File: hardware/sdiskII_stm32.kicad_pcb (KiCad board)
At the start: 2 copper layers, 76 x 56.3 mm, 23 parts, among them J1 PWR, J2 APPLE_SDISKII, J3 Conn_01x06, J4 UART, J5 Conn_01x04, J6 STLINK, U2 MicroSD_SDIO, U8 DM-OLED096-636

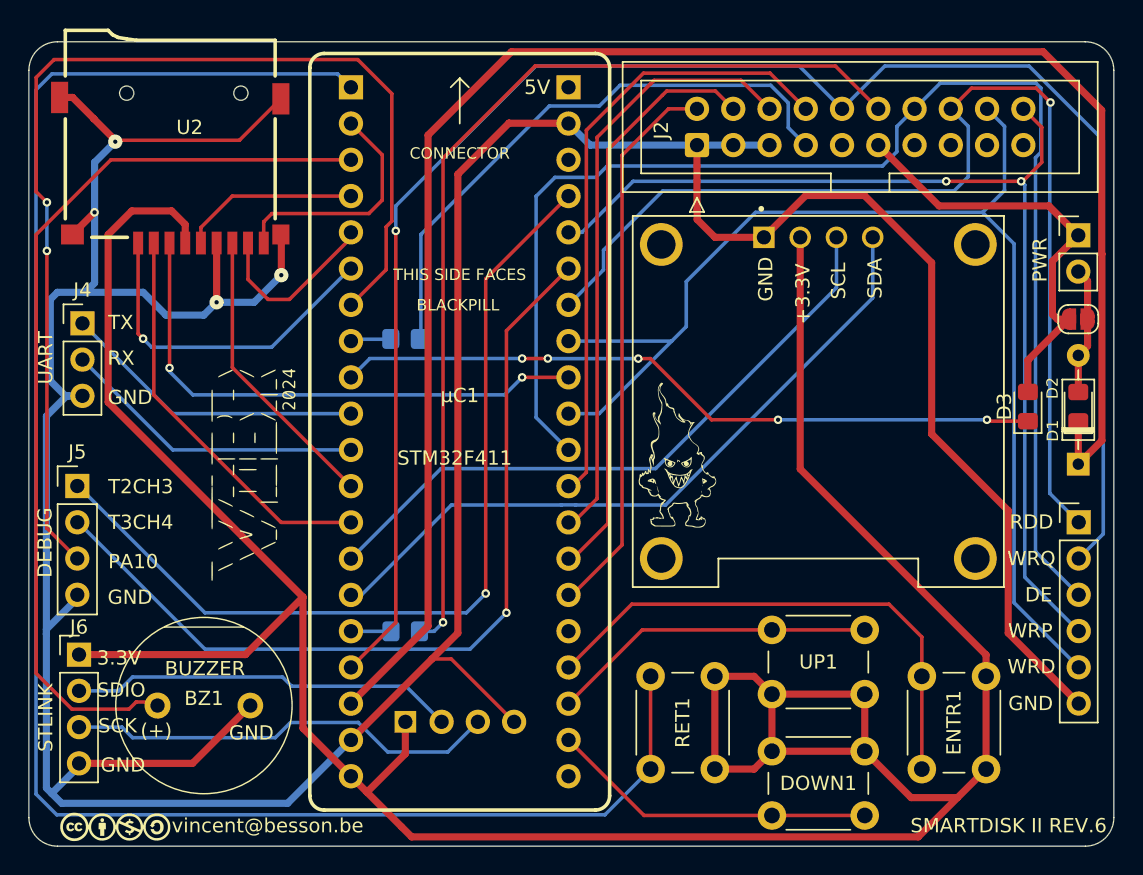
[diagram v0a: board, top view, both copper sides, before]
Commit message: fixing Smartport on IIe II+ Rev6 Hardware
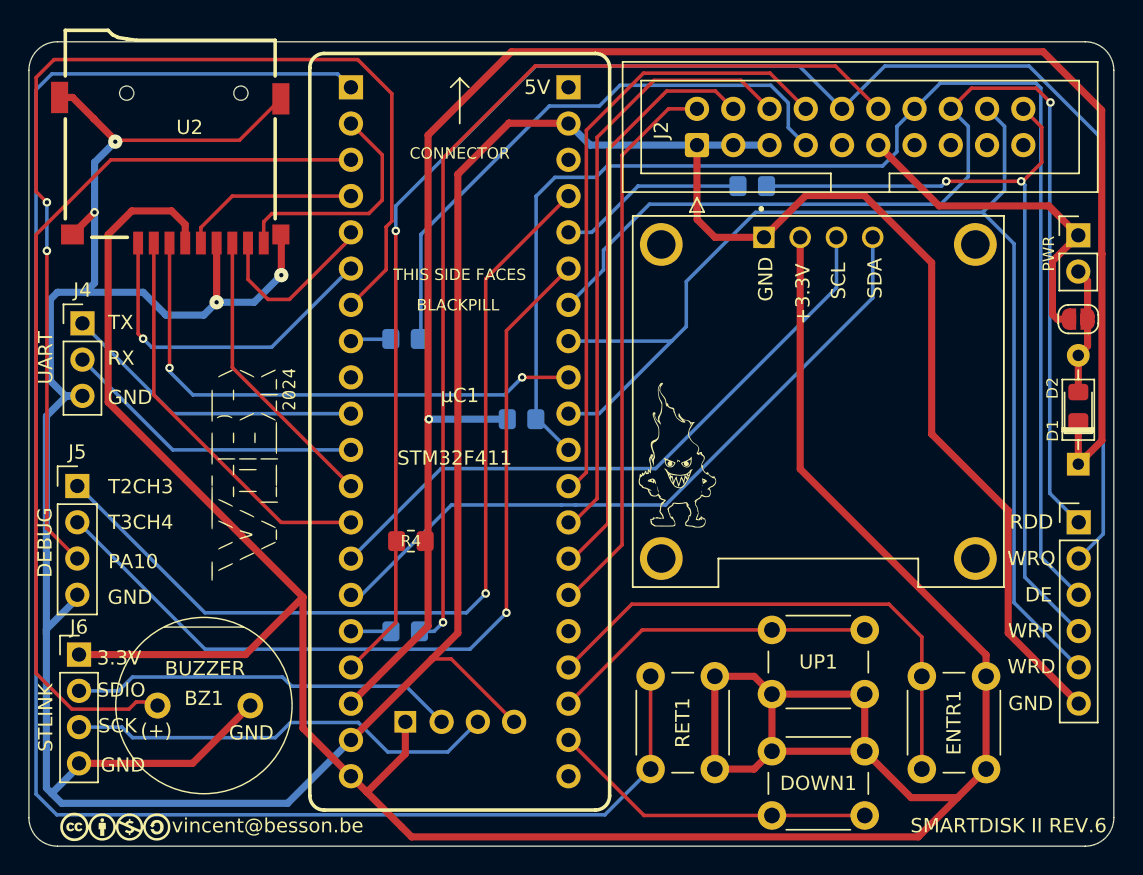
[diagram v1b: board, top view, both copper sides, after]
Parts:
- removed D3: 1N4148WT, Diode_SMD:D_0805_2012Metric_Pad1.15x1.40mm_HandSolder
- added R1: 330, Resistor_SMD:R_0805_2012Metric_Pad1.20x1.40mm_HandSolder, B.Cu at (182.2, 95.4)
- added R4: 1K5, Resistor_SMD:R_0805_2012Metric_Pad1.20x1.40mm_HandSolder, F.Cu at (158.2, 120.2)
- added R5: 1K5, Resistor_SMD:R_0805_2012Metric_Pad1.20x1.40mm_HandSolder, B.Cu at (166.0, 111.7)
- renumbered R5 to R2, R4 to R3
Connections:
- J2 pad 20: WR_PROTECT -> WR_PROTECT_D
- J3 pad 4: WR_PROTECT -> WR_PROTECT_D
- μC1 pad 9: A2PWR -> unconnected-(μC1-A12-Pad9)
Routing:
- net WR_PROTECT: track 72.6 -> 13.2 mm, vias 2 -> 0
- net WR_PROTECT_D: track 0.00 -> 57.4 mm, vias 0 -> 2
- net A2PWR: track 49.8 -> 0.00 mm, vias 5 -> 0
- net VCC: track 30.7 -> 24.4 mm
- net PWR_IN: track 121.9 -> 127.4 mm, vias 0 -> 1
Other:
- board text added: "REV6: (beta) #2 - Adding R6 on WR_PROTECT for future use - Adding PUP On DEVICE_ENABLE, WR_REQ - Adding D3, to avoid PA12 -> Apple PWR supply REV5: (beta) - Adding D1 & D2 protection (only one is needed), - Adding more GND to SDCARD - Adding R4 PIN SELECT for protection on DISK3.5 use - Adding R5 PIN SELECT for protection on DISK3.5 use REV4: (Last production & tested version) - Adding PWR pads -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"
- board text removed: "REV6: (beta) - Adding A2PWR PA12, Apple II PWR check on external PWR supply - Adding D3, to avoid PA12 -> Apple PWR supply REV5: (beta) - Adding D1 & D2 protection (only one is needed), - Adding more GND to SDCARD - Adding R4 PIN SELECT for protection on DISK3.5 use - Adding R5 PIN SELECT for protection on DISK3.5 use REV4: (Last production & tested version) - Adding PWR pads - Moving SDCard"

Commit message: Board rev7 beta
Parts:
- removed the   at (147.0, 115.5)
- added 3V: SPST, Jumper:SolderJumper-2_P1.3mm_Open_RoundedPad1.0x1.5mm, F.Cu at (142.1, 121.2)
- added 3V: PWR, Connector_PinHeader_2.54mm:PinHeader_1x02_P2.54mm_Vertical, F.Cu at (138.7, 122.7)
- added C1: 10uF, Capacitor_SMD:C_0805_2012Metric_Pad1.18x1.45mm_HandSolder, F.Cu at (138.4, 116.0)
- added C2: 10uF, Capacitor_SMD:C_0805_2012Metric_Pad1.18x1.45mm_HandSolder, F.Cu at (149.4, 106.7)
- added Fu2: Polyfuse 500mA, Fuse:Fuse_0805_2012Metric_Pad1.15x1.40mm_HandSolder, F.Cu at (204.7, 109.4)
- added G***: LOGO, LOGO, B.Cu at (200.6, 137.6)
- added LM1117/33: LM1117MP-3.3, Package_TO_SOT_SMD:SOT-223-3_TabPin2, F.Cu at (143.5, 113.4)
- moved JP1 62.2 mm to (145.0, 121.2), turned to -90 degrees
- moved J1 61.4 mm to (148.4, 122.7), turned to 180 degrees
- moved G*** 32.6 mm to (203.9, 133.5)
- moved D1 16.9 mm to (204.7, 97.9), turned to -90 degrees
- moved D2 8.89 mm to (204.7, 101.9), turned to -90 degrees
- moved J3 4.94 mm to (204.7, 114.0)
- moved R4 0.36 mm to (157.9, 120.3)
- moved J4 0.33 mm to (134.9, 105.0)
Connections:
- D1 pad 1: PWR_IN -> PWR_RD
- D1 pad 2: PWR_RD -> Net-(D1-A)
- D2 pad 1: PWR_IN -> PWR_RD
- D2 pad 2: PWR_RD -> Net-(D1-A)
- J1 pad 1: VCC -> PWR_5VIN
- JP1 pad 2: VCC -> PWR_5VIN
- R4 pad 2: PWR_IN -> PWR_RD
- R5 pad 2: PWR_IN -> PWR_RD
- U2 pad : (no net) -> GND
- U2 pad ~: (no net) -> GND
- μC1 pad 18: PWR_IN -> PWR_5VIN
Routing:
- net PWR_IN: track 127.4 -> 0.00 mm, vias 1 -> 0
- net PWR_RD: track 9.38 -> 136.3 mm, vias 0 -> 2
- net Net-(J7-Pin_2): track 0.00 -> 17.6 mm
- net PWR_5VIN: track 0.00 -> 15.1 mm
- net GND: track 272.6 -> 280.0 mm
- net Net-(D1-A): track 0.00 -> 5.79 mm
- net WR_PROTECT_D: track 57.4 -> 52.2 mm
- net WR_DATA: track 88.3 -> 83.2 mm
- net WR_REQ: track 121.9 -> 117.1 mm
- net RD_DATA: track 76.5 -> 71.9 mm
- net DEVICE_ENABLE: track 95.1 -> 90.5 mm
- net SDIO_D2: track 23.9 -> 20.5 mm
- net TIM3_CH4: track 60.2 -> 62.9 mm
- net VCC: track 24.4 -> 27.0 mm
- net SDIO_CMD: track 38.1 -> 36.1 mm
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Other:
- board text added: "10uF"
- board text added: "1K5"
- board text added: "330R"
- board text added: "5V"
- board text added: "FUSE"
- board text added: "OR"
- board text added: "REV7: - Add LM1117 to power the stm32,SDCARD, OLED - Add jumper / pads to select power source - Add resettable fuse on 5V rail REV6: (beta) #2 - Adding R6 on WR_PROTECT for future use - Adding PUP On DEVICE_ENABLE, WR_REQ - Adding D3, to avoid PA12 -> Apple PWR supply REV5: (beta) - Adding D1 & D2 protection (only one is needed), - Adding more GND to SDCARD - Adding R4 PIN SELECT for protection o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"
- board text added: "SELECT"
- board text added: "SMARTDISK II REV.7"
- board text added: "WARNING: only 1 PWR SRC - 3V - 5V - SDIO 3V DEBUG PINOUT: - TIM2CH3 - TIM3CH4 - DEBUG (A10) - GND"
- board text removed: "PA10"
- board text removed: "PWR"
- board text removed: "REV6: (beta) #2 - Adding R6 on WR_PROTECT for future use - Adding PUP On DEVICE_ENABLE, WR_REQ - Adding D3, to avoid PA12 -> Apple PWR supply REV5: (beta) - Adding D1 & D2 protection (only one is needed), - Adding more GND to SDCARD - Adding R4 PIN SELECT for protection on DISK3.5 use - Adding R5 PIN SELECT for protection on DISK3.5 use REV4: (Last production & tested version) - Adding PWR pads -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"
- board text removed: "SMARTDISK II REV.6"
- board text removed: "T2CH3"
- board text removed: "T3CH4"

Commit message: v0.80.17 Alpha
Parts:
- added BYP: BYP, Jumper:SolderJumper-2_P1.3mm_Open_RoundedPad1.0x1.5mm, F.Cu at (204.7, 112.8)
- J3: value Conn_01x06 -> A2PIN
- J5: value Conn_01x04 -> DEBUG
- R1, R2, R3: value 330 -> 330R
- moved J3 2.19 mm to (204.7, 116.2)
- moved G*** 1.42 mm to (203.5, 134.8)
- moved Fu2 0.28 mm to (204.7, 109.1)
- renumbered 3V to J7, LM1117/33 to U1
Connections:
- U2 pad : GND -> (no net)
- U2 pad ~: GND -> (no net)
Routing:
- net Net-(D1-A): track 5.79 -> 11.5 mm
- net VCC: track 27.0 -> 31.4 mm
- net GND: track 280.0 -> 282.5 mm
- net WR_REQ: track 117.1 -> 119.3 mm
- net WR_PROTECT_D: track 52.2 -> 54.4 mm
- net DEVICE_ENABLE: track 90.5 -> 92.7 mm
- net WR_DATA: track 83.2 -> 85.4 mm
- net RD_DATA: track 71.9 -> 74.1 mm
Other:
- board text added: "3V"
- board text added: "REV7: - Add LM1117 to power the stm32,SDCARD, OLED - Add jumper / pads to select power source - Add resettable fuse on 5V rail (with a bypass pad) - Silk adjustment REV6: (beta) #2 - Adding R6 on WR_PROTECT for future use - Adding PUP On DEVICE_ENABLE, WR_REQ - Adding D3, to avoid PA12 -> Apple PWR supply REV5: (beta) - Adding D1 & D2 protection (only one is needed), - Adding more GND to SDCARD -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"
- board text added: "WARNING: ONLY 1 PWR SRC - 3V - 5V - SDIO 3V DEBUG PINOUT: - TIM2CH3 - TIM3CH4 - DEBUG (A10) - GND"
- board text removed: "REV7: - Add LM1117 to power the stm32,SDCARD, OLED - Add jumper / pads to select power source - Add resettable fuse on 5V rail REV6: (beta) #2 - Adding R6 on WR_PROTECT for future use - Adding PUP On DEVICE_ENABLE, WR_REQ - Adding D3, to avoid PA12 -> Apple PWR supply REV5: (beta) - Adding D1 & D2 protection (only one is needed), - Adding more GND to SDCARD - Adding R4 PIN SELECT for protection o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"
- board text removed: "WARNING: only 1 PWR SRC - 3V - 5V - SDIO 3V DEBUG PINOUT: - TIM2CH3 - TIM3CH4 - DEBUG (A10) - GND"

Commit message: Board Rev7 beta 2 # Add bypass pads
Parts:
- added BPR1: BYP, Jumper:SolderJumper-2_P1.3mm_Open_RoundedPad1.0x1.5mm, B.Cu at (178.8, 96.1)
- added BPR2: BYP, Jumper:SolderJumper-2_P1.3mm_Open_RoundedPad1.0x1.5mm, B.Cu at (157.8, 102.8)
- added BPR3: BYP, Jumper:SolderJumper-2_P1.3mm_Open_RoundedPad1.0x1.5mm, B.Cu at (157.8, 123.3)
- renumbered 3V to JP2, BYP to JP3
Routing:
- net WR_PROTECT_D: track 54.4 -> 59.6 mm
- net SELECT: track 2.80 -> 7.53 mm, vias 0 -> 1
- net 3.5DSK: track 2.67 -> 6.23 mm
- net SELECT_D: track 69.0 -> 71.5 mm, vias 1 -> 2
- net GND: track 282.5 -> 283.5 mm
- net RD_DATA: track 74.1 -> 73.3 mm
- net 3.5DSK_D: track 41.5 -> 42.0 mm
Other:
- board text added: "REV7: - Add LM1117 to power the stm32,SDCARD, OLED - Add jumper / pads to select power source - Add resettable fuse on 5V rail (with a bypass pad) - Add Bypass pad for Resistors - Silk adjustment REV6: (beta) #2 - Adding R6 on WR_PROTECT for future use - Adding PUP On DEVICE_ENABLE, WR_REQ - Adding D3, to avoid PA12 -> Apple PWR supply REV5: (beta) - Adding D1 & D2 protection (only one is needed)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"
- board text removed: "REV7: - Add LM1117 to power the stm32,SDCARD, OLED - Add jumper / pads to select power source - Add resettable fuse on 5V rail (with a bypass pad) - Silk adjustment REV6: (beta) #2 - Adding R6 on WR_PROTECT for future use - Adding PUP On DEVICE_ENABLE, WR_REQ - Adding D3, to avoid PA12 -> Apple PWR supply REV5: (beta) - Adding D1 & D2 protection (only one is needed), - Adding more GND to SDCARD -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"

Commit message: 0.80.17 beta 4
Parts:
- renumbered JP2 to 3V, JP3 to BPF
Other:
- board text added: "Fu1"
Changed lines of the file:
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@@
 		(descr "SMD Solder Jumper, 1x1.5mm, rounded Pads, 0.3mm gap, open")
 		(tags "solder jumper open")
-		(property "Reference" "JP2"
+		(property "Reference" "3V"
 			(at 2.34 0.06 180)
 			(layer "F.SilkS")
@@
 		(descr "SMD Solder Jumper, 1x1.5mm, rounded Pads, 0.3mm gap, open")
 		(tags "solder jumper open")
-		(property "Reference" "JP3"
+		(property "Reference" "BPF"
 			(at 2.22 0.23 90)
 			(layer "F.SilkS")
@@
 				(font
 					(size 0.8 0.8)
-					(thickness 0.15)
+					(thickness 0.16)
+					(bold yes)
 				)
 			)
@@
 			(font
 				(size 0.8 0.8)
-				(thickness 0.1875)
+				(thickness 0.16)
+				(bold yes)
 			)
 			(justify left bottom)
@@
 		)
 	)
+	(gr_text "Fu1\n"
+		(at 206.8 110.71 90)
+		(layer "F.SilkS")
+		(effects
+			(font
+				(size 0.8 0.8)
+				(thickness 0.1875)
+			)
+			(justify left bottom)
+		)
+	)
 	(gr_text "GND"
 		(at 136.18 110.58 0)
@@
 	)
 	(segment
-		(start 132.75 99.9)
-		(end 132.75 119.33)
+		(start 132 95.75)
+		(end 132 87.75)
 		(width 0.25)
 		(layer "F.Cu")
@@
 	)
 	(segment
-		(start 132 87.75)
-		(end 132 95.75)
+		(start 132.75 119.33)
+		(end 135 121.58)
 		(width 0.25)
 		(layer "F.Cu")
@@
 	)
 	(segment
-		(start 132 95.75)
-		(end 132.75 96.5)
+		(start 132.742702 97.052702)
+		(end 132.742702 96.492702)
+		(width 0.25)
+		(layer "F.Cu")
+		(net 37)
+	)
+	(segment
+		(start 132.769798 98.934798)
+		(end 132.75 98.954596)
 		(width 0.25)
 		(layer "F.Cu")
@@
 	)
 	(segment
-		(start 149.39 86.5)
+		(start 132 87.75)
 		(end 133.25 86.5)
 		(width 0.25)
@@
 	)
 	(segment
-		(start 133.25 86.5)
-		(end 132 87.75)
+		(start 132.75 98.954596)
+		(end 132.75 119.33)
 		(width 0.25)
 		(layer "F.Cu")
@@
 	)
 	(segment
-		(start 132.75 119.33)
-		(end 135 121.58)
+		(start 132.742702 96.492702)
+		(end 132 95.75)
+		(width 0.25)
+		(layer "F.Cu")
+		(net 37)
+	)
+	(segment
+		(start 133.25 86.5)
+		(end 149.39 86.5)
 		(width 0.25)
 		(layer "F.Cu")
@@
 	)
 	(via
-		(at 132.75 99.9)
+		(at 132.769798 98.934798)
 		(size 0.6)
 		(drill 0.3)
@@
 	)
 	(via
-		(at 132.75 96.5)
+		(at 132.742702 97.052702)
 		(size 0.6)
 		(drill 0.3)
@@
 	)
 	(segment
-		(start 156.515 101.215)
-		(end 156.515 88.488883)
+		(start 132.742702 97.052702)
+		(end 132.75 97.06)
 		(width 0.25)
 		(layer "B.Cu")
@@
 	)
 	(segment
-		(start 132.75 99.9)
-		(end 132.75 96.5)
+		(start 132.75 97.06)
+		(end 132.75 98.915)
+		(width 0.25)
+		(layer "B.Cu")
+		(net 37)
+	)
+	(segment
+		(start 132.75 98.915)
+		(end 132.769798 98.934798)
+		(width 0.25)
+		(layer "B.Cu")
+		(net 37)
+	)
+	(segment
+		(start 156.515 101.215)
+		(end 156.515 88.488883)
 		(width 0.25)
 		(layer "B.Cu")

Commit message: PCB Board v7 Adjust + 3D Print Case
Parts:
- G***: moved to B.Cu
- moved G*** 26.2 mm to (196.1, 109.7), turned to 180 degrees
- moved G*** 22.7 mm to (191.6, 116.8)
- moved D1 5.02 mm to (204.8, 102.9)
- moved D2 5.02 mm to (204.8, 107.0)
- moved Fu2 4.70 mm to (204.8, 113.8)
- moved J3 4.52 mm to (204.7, 120.7)
- moved BPF 4.48 mm to (204.7, 117.3)
- moved JP1 3.85 mm to (148.8, 121.6)
- moved 3V 3.85 mm to (138.3, 121.6)
- moved J1 2.94 mm to (145.5, 122.8)
- moved J7 2.89 mm to (141.6, 122.8)
- moved U1 0.59 mm to (143.5, 112.8)
- moved R4 0.09 mm to (157.8, 120.3)
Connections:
- U2 pad : (no net) -> GND
- U2 pad ~: (no net) -> GND
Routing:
- net VCC: track 31.4 -> 36.7 mm
- net PWR_RD: track 136.3 -> 141.3 mm
- net RD_DATA: track 73.3 -> 77.8 mm
- net WR_PROTECT_D: track 59.6 -> 64.2 mm
- net WR_DATA: track 85.4 -> 89.9 mm
- net DEVICE_ENABLE: track 92.7 -> 97.3 mm
- net WR_REQ: track 119.3 -> 123.8 mm
- net GND: track 283.5 -> 287.2 mm
- net TIM2_CH3: track 62.6 -> 65.7 mm
- net +3.3V: track 211.8 -> 210.0 mm
- net Net-(J7-Pin_2): track 17.6 -> 19.3 mm
- net Net-(D1-A): track 11.5 -> 10.0 mm
- net PWR_5VIN: track 15.1 -> 16.0 mm
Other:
- board text removed: "3.3V"

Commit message: Board Rev7 to test production
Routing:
- net VCC: track 36.7 -> 37.3 mm
